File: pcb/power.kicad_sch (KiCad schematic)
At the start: 20 parts, among them U5 REG_LDO_3V3_250mA_TI_LP5907MF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, U7 REG_SW_BOOST_TI_TLV61046ADBV

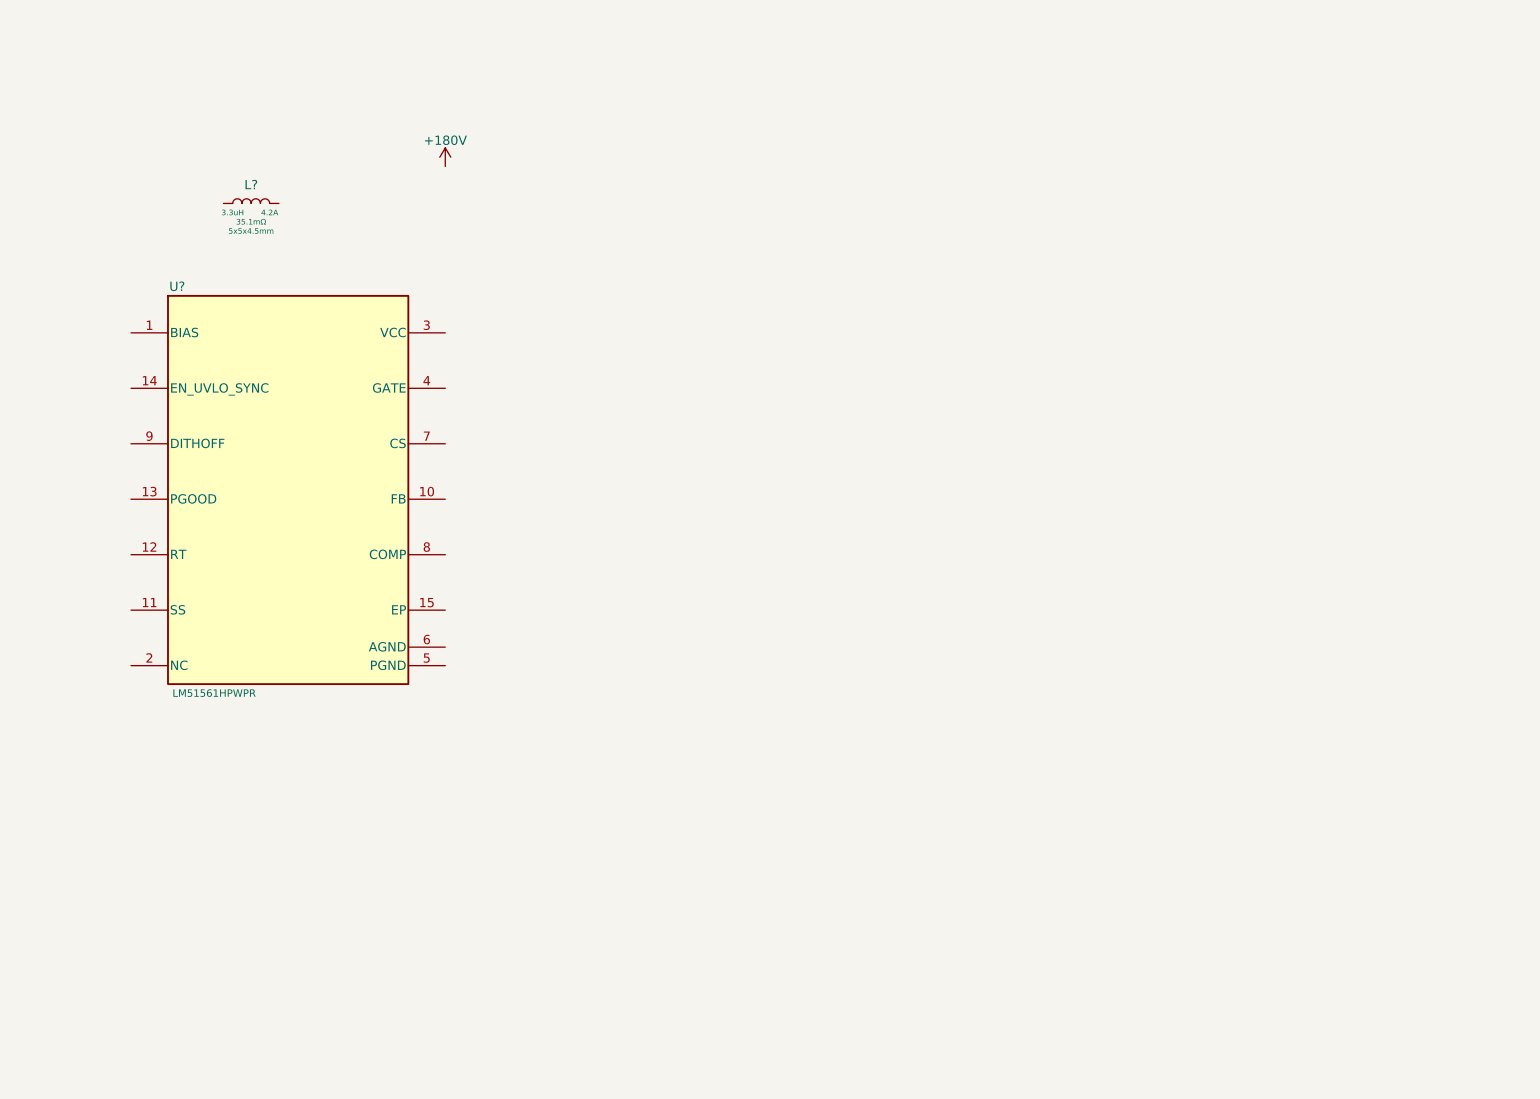
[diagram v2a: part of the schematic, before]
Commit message: Added FET, shunt, and shunt filter
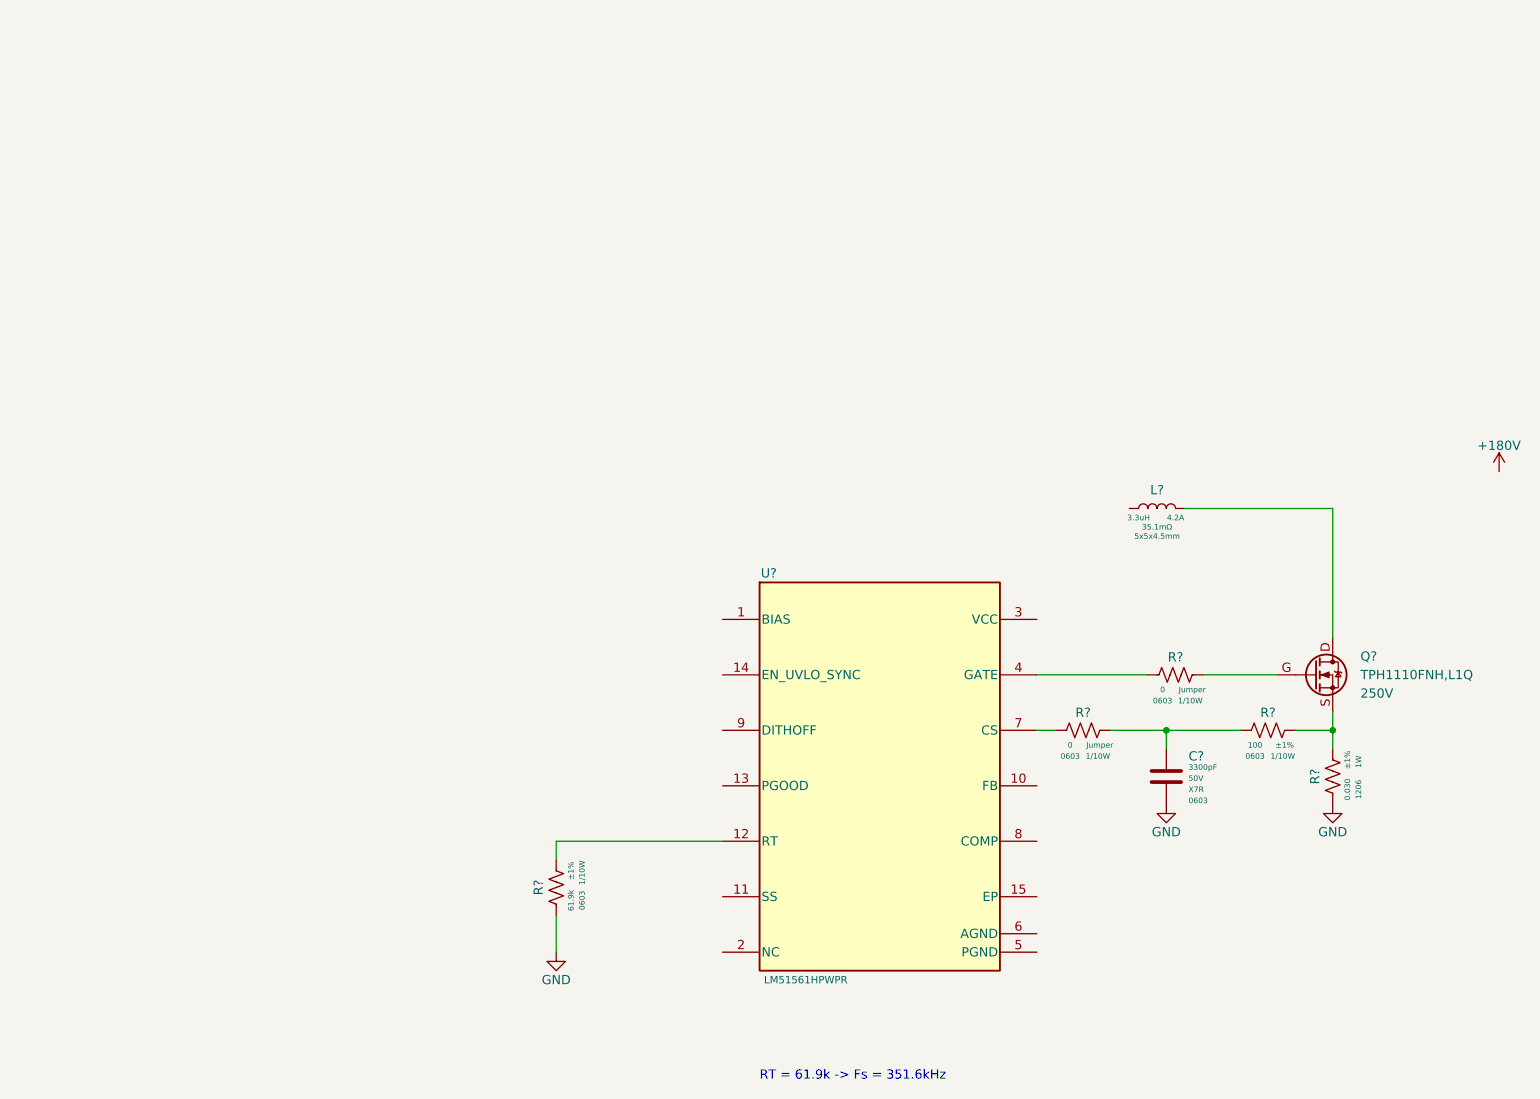
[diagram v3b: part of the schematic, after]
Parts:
- added C?: CAP_CER_3300p_50V_X7R_0603, Capacitor_SMD:C_0603_1608Metric, symbol .arjun:CAP_CER_3300p_50V_X7R_0603
- added Q?: NFET_250V_10A_TPH1110FNH,L1Q, arjun_footprints:SOP Advance_TOS, symbol .arjun:NFET_250V_10A_TPH1110FNH,L1Q
- added R?: RES_61K9_1P_1/10W_0603, Resistor_SMD:R_0603_1608Metric, symbol .arjun:RES_61K9_1P_1/10W_0603
- added R? (x2): RES_0R_1/10W_0603, Resistor_SMD:R_0603_1608Metric, symbol .arjun:RES_0R_1/10W_0603
- added R?: RES_100R_1P_1/10W_0603, Resistor_SMD:R_0603_1608Metric, symbol .arjun:RES_100R_1P_1/10W_0603
- added R?: RES_R030_1P_1W_1206, Resistor_SMD:R_1206_3216Metric, symbol .arjun:RES_R030_1P_1W_1206
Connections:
- net GND: now also C?.2, R?.2, R?.2
- net at U?.12 (RT): now also R?.1
- net at U?.4 (GATE): now also R?.2
- net at U?.7 (CS): now also R?.2
- net at L?.2: now also Q?.D
- new net: C?.1, R?.1, R?.2
- new net: Q?.G, R?.1
- new net: Q?.S, R?.1, R?.1
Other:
- note added: "RT = 61.9k -> Fs = 351.6kHz"
- moved on the sheet: L?, U?

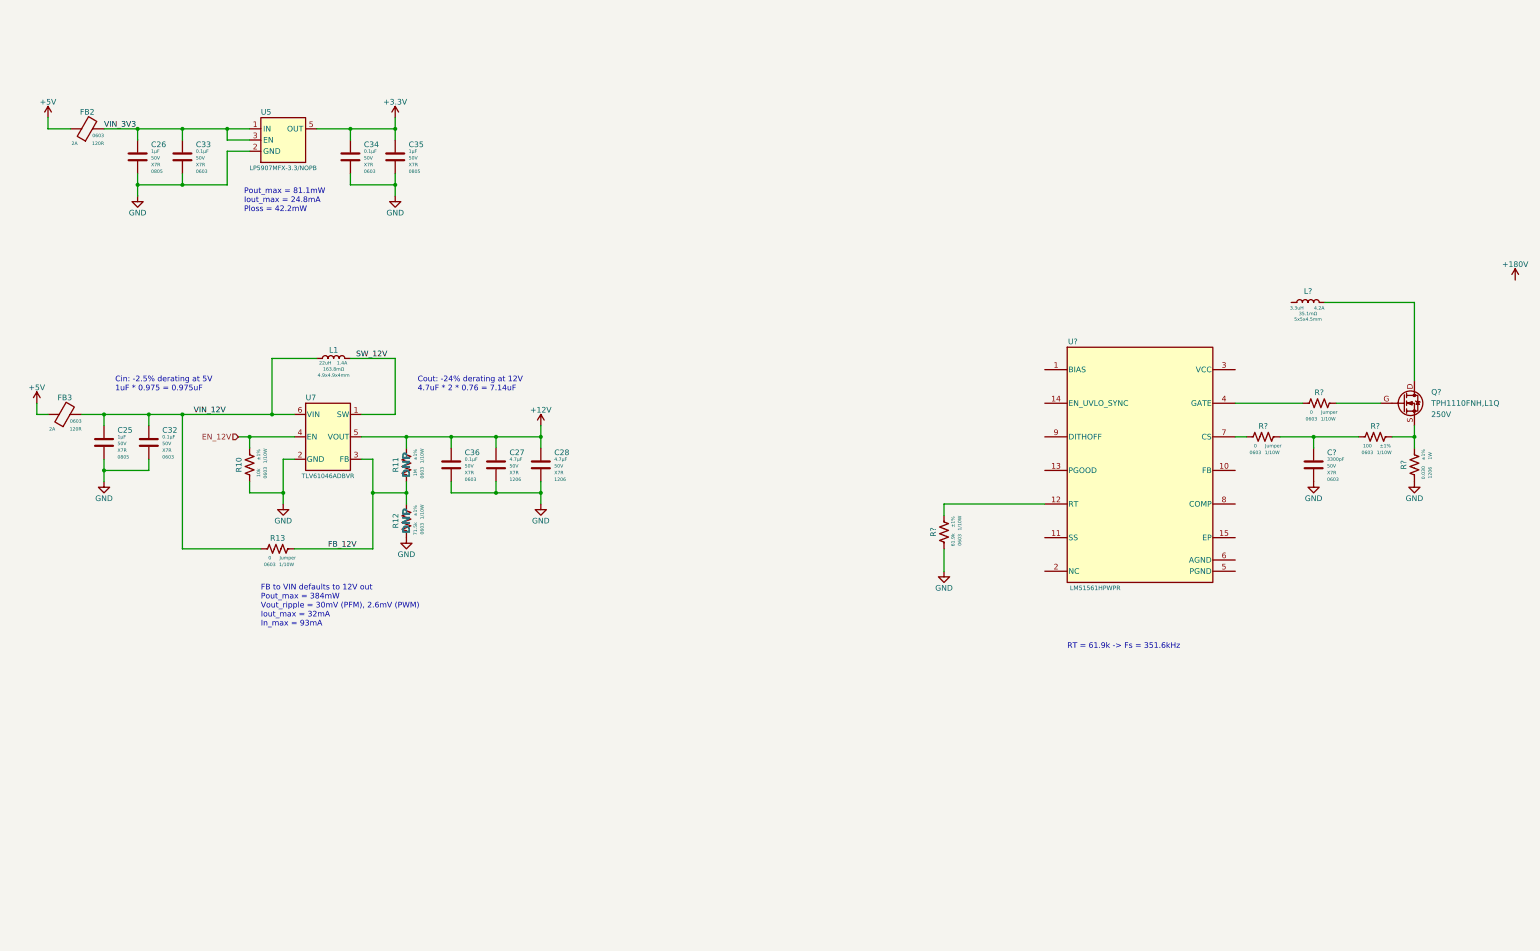
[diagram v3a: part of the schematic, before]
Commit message: Added Diode and output caps to 180V Boost
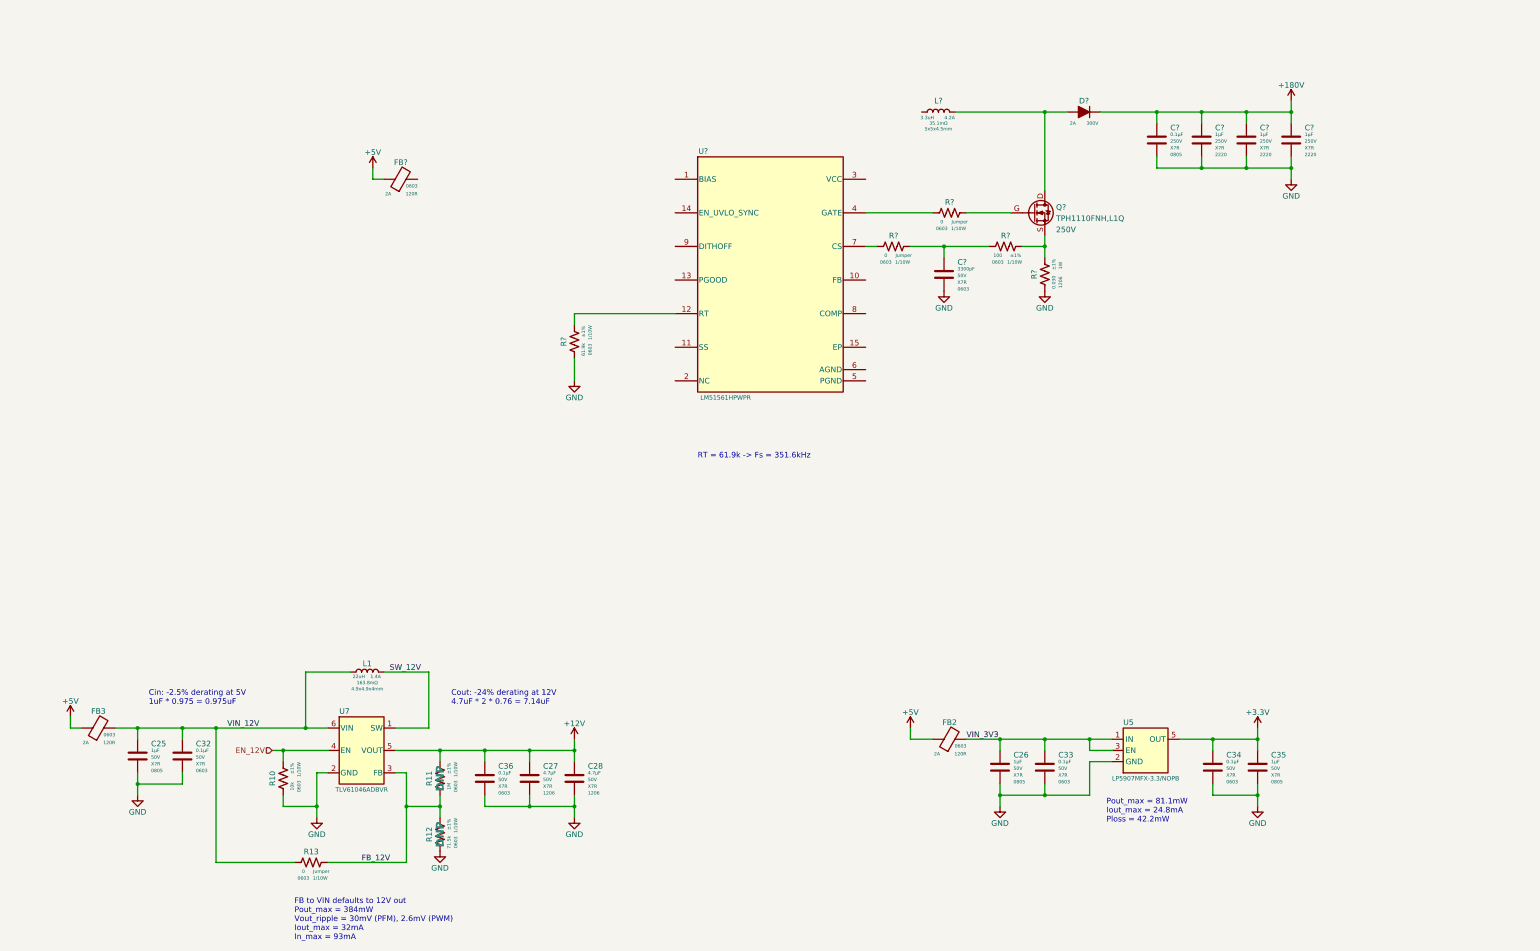
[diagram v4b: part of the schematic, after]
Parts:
- removed Q?: NFET_250V_10A_TPH1110FNH,L1Q, arjun_footprints:SOP Advance_TOS, symbol .arjun:NFET_250V_10A_TPH1110FNH,L1Q
- added C? (x3): CAP_CER_1u_250V_X7R_2220, Capacitor_SMD:C_2220_5650Metric, symbol .arjun:CAP_CER_1u_250V_X7R_2220
- added C?: CAP_CER_0u1_250V_X7R_0805, Capacitor_SMD:C_0805_2012Metric, symbol .arjun:CAP_CER_0u1_250V_X7R_0805
- added D?: D_300V_2A_SMB, Diode_SMD:D_SMB, symbol .arjun:D_300V_2A_SMB
- added FB?: FER_120R_2A_0603, Inductor_SMD:L_0603_1608Metric, symbol .arjun:FER_120R_2A_0603
- added Q?: NFET_250V_10A_TPH1110FNH,L1Q, arjun_footprints:SOP Advance_TOS, symbol .arjun:NFET_250V_10A_TPH1110FNH,L1Q
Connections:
- net +5V: now also FB?.1
- net 180V: now also C?.1, C?.1, C?.1, C?.1, D?.1 (K)
- net GND: now also C?.2, C?.2, C?.2, C?.2
- net at L?.2: now also D?.2 (A), Q?.D
- net at R?.1: now also Q?.G
- net at R?.1, R?.1: now also Q?.S
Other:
- moved on the sheet: C25, C26, C27, C28, C32, C33, C34, C35, C36, C?, FB2, FB3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
